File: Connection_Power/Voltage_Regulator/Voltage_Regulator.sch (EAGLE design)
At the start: 7 parts, among them IC2 TS1117

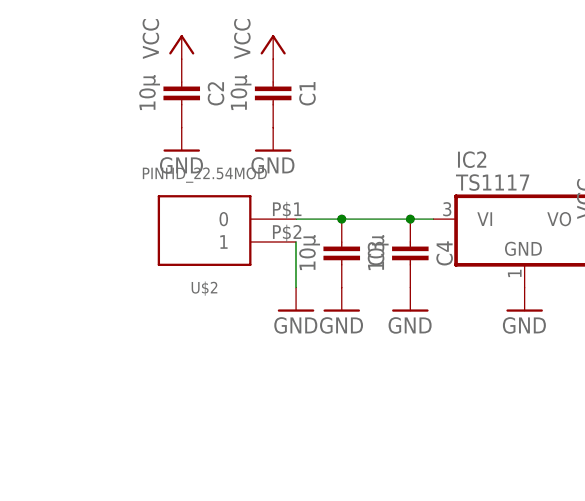
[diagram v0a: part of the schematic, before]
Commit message: Update Pinheader
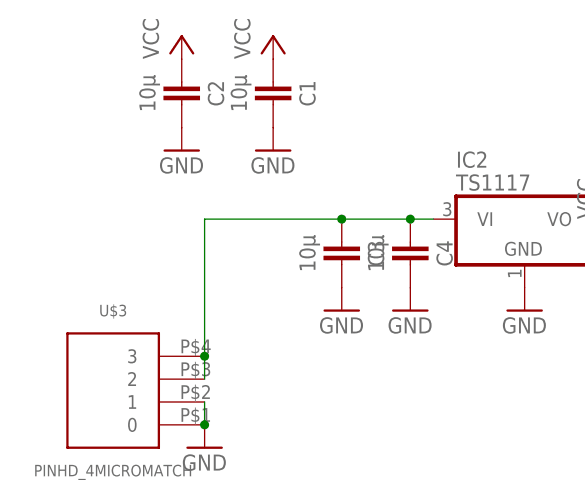
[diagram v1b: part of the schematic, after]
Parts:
- removed U$2: PINHD_22.54MOD, thar:PINHD_22.54MOD
- added U$3: PINHD_4MICROMATCH, thar:PINHD_4MICROMATCH
- C1, C2, C3, C4: device thar:CAPACITOR1206 -> thar:CAPACITOR
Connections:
- net GND: now also U$3.0, U$3.1; no longer U$2.1
- net N$2: now also U$3.2, U$3.3; no longer U$2.0
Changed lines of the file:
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@@
 <grid distance="0.1" unitdist="inch" unit="inch" style="lines" multiple="1" display="no" altdistance="0.01" altunitdist="inch" altunit="inch"/>
 <layers>
-<layer number="1" name="Top" color="4" fill="1" visible="yes" active="no"/>
-<layer number="16" name="Bottom" color="1" fill="1" visible="yes" active="no"/>
-<layer number="17" name="Pads" color="2" fill="1" visible="yes" active="no"/>
-<layer number="18" name="Vias" color="2" fill="1" visible="yes" active="no"/>
-<layer number="19" name="Unrouted" color="6" fill="1" visible="yes" active="no"/>
-<layer number="20" name="Dimension" color="15" fill="1" visible="yes" active="no"/>
-<layer number="21" name="tPlace" color="7" fill="1" visible="yes" active="no"/>
-<layer number="22" name="bPlace" color="7" fill="1" visible="yes" active="no"/>
-<layer number="23" name="tOrigins" color="15" fill="1" visible="yes" active="no"/>
-<layer number="24" name="bOrigins" color="15" fill="1" visible="yes" active="no"/>
-<layer number="25" name="tNames" color="7" fill="1" visible="yes" active="no"/>
-<layer number="26" name="bNames" color="7" fill="1" visible="yes" active="no"/>
-<layer number="27" name="tValues" color="7" fill="1" visible="yes" active="no"/>
-<layer number="28" name="bValues" color="7" fill="1" visible="yes" active="no"/>
+<layer number="1" name="Top" color="4" fill="1" visible="no" active="no"/>
+<layer number="16" name="Bottom" color="1" fill="1" visible="no" active="no"/>
+<layer number="17" name="Pads" color="2" fill="1" visible="no" active="no"/>
+<layer number="18" name="Vias" color="2" fill="1" visible="no" active="no"/>
+<layer number="19" name="Unrouted" color="6" fill="1" visible="no" active="no"/>
+<layer number="20" name="Dimension" color="15" fill="1" visible="no" active="no"/>
+<layer number="21" name="tPlace" color="7" fill="1" visible="no" active="no"/>
+<layer number="22" name="bPlace" color="7" fill="1" visible="no" active="no"/>
+<layer number="23" name="tOrigins" color="15" fill="1" visible="no" active="no"/>
+<layer number="24" name="bOrigins" color="15" fill="1" visible="no" active="no"/>
+<layer number="25" name="tNames" color="7" fill="1" visible="no" active="no"/>
+<layer number="26" name="bNames" color="7" fill="1" visible="no" active="no"/>
+<layer number="27" name="tValues" color="7" fill="1" visible="no" active="no"/>
+<layer number="28" name="bValues" color="7" fill="1" visible="no" active="no"/>
 <layer number="29" name="tStop" color="7" fill="3" visible="no" active="no"/>
 <layer number="30" name="bStop" color="7" fill="6" visible="no" active="no"/>
@@
 <layer number="35" name="tGlue" color="7" fill="4" visible="no" active="no"/>
 <layer number="36" name="bGlue" color="7" fill="5" visible="no" active="no"/>
-<layer number="37" name="tTest" color="7" fill="1" visible="yes" active="no"/>
-<layer number="38" name="bTest" color="7" fill="1" visible="yes" active="no"/>
+<layer number="37" name="tTest" color="7" fill="1" visible="no" active="no"/>
+<layer number="38" name="bTest" color="7" fill="1" visible="no" active="no"/>
 <layer number="39" name="tKeepout" color="4" fill="11" visible="no" active="no"/>
 <layer number="40" name="bKeepout" color="1" fill="11" visible="no" active="no"/>
@@
 <layer number="44" name="Drills" color="7" fill="1" visible="no" active="no"/>
 <layer number="45" name="Holes" color="7" fill="1" visible="no" active="no"/>
-<layer number="46" name="Milling" color="3" fill="1" visible="yes" active="no"/>
-<layer number="47" name="Measures" color="7" fill="1" visible="yes" active="no"/>
-<layer number="48" name="Document" color="7" fill="1" visible="yes" active="no"/>
-<layer number="49" name="Reference" color="7" fill="1" visible="yes" active="no"/>
-<layer number="50" name="dxf" color="7" fill="1" visible="yes" active="no"/>
-<layer number="51" name="tDocu" color="7" fill="1" visible="yes" active="no"/>
-<layer number="52" name="bDocu" color="7" fill="1" visible="yes" active="no"/>
-<layer number="53" name="tGND_GNDA" color="7" fill="9" visible="yes" active="no"/>
-<layer number="54" name="bGND_GNDA" color="1" fill="9" visible="yes" active="no"/>
-<layer number="56" name="wert" color="7" fill="1" visible="yes" active="no"/>
-<layer number="57" name="tCAD" color="7" fill="1" visible="yes" active="no"/>
+<layer number="46" name="Milling" color="3" fill="1" visible="no" active="no"/>
+<layer number="47" name="Measures" color="7" fill="1" visible="no" active="no"/>
+<layer number="48" name="Document" color="7" fill="1" visible="no" active="no"/>
+<layer number="49" name="Reference" color="7" fill="1" visible="no" active="no"/>
+<layer number="50" name="dxf" color="7" fill="1" visible="no" active="no"/>
+<layer number="51" name="tDocu" color="7" fill="1" visible="no" active="no"/>
+<layer number="52" name="bDocu" color="7" fill="1" visible="no" active="no"/>
+<layer number="53" name="tGND_GNDA" color="7" fill="9" visible="no" active="no"/>
+<layer number="54" name="bGND_GNDA" color="1" fill="9" visible="no" active="no"/>
+<layer number="56" name="wert" color="7" fill="1" visible="no" active="no"/>
+<layer number="57" name="tCAD" color="7" fill="1" visible="no" active="no"/>
+<layer number="90" name="Modules" color="5" fill="1" visible="no" active="no"/>
 <layer number="91" name="Nets" color="2" fill="1" visible="yes" active="yes"/>
 <layer number="92" name="Busses" color="1" fill="1" visible="yes" active="yes"/>
@@
 <layer number="97" name="Info" color="7" fill="1" visible="yes" active="yes"/>
 <layer number="98" name="Guide" color="6" fill="1" visible="yes" active="yes"/>
+<layer number="99" name="SpiceOrder" color="7" fill="1" visible="no" active="no"/>
 <layer number="100" name="Muster" color="7" fill="1" visible="no" active="no"/>
 <layer number="101" name="Patch_Top" color="12" fill="4" visible="yes" active="yes"/>
@@
 <layer number="111" name="LPC17xx" color="7" fill="1" visible="no" active="yes"/>
 <layer number="112" name="tSilk" color="7" fill="1" visible="no" active="yes"/>
+<layer number="113" name="IDFDebug" color="7" fill="1" visible="yes" active="yes"/>
 <layer number="116" name="Patch_BOT" color="9" fill="4" visible="yes" active="yes"/>
 <layer number="118" name="Rect_Pads" color="7" fill="1" visible="no" active="yes"/>
@@
 <part name="GND2" library="supply1" deviceset="GND" device=""/>
 <part name="P+3" library="supply1" deviceset="VCC" device=""/>
-<part name="C2" library="thar" deviceset="CAPACITOR" device="1206" value="10µ"/>
-<part name="GND4" library="supply1" deviceset="GND" device=""/>
-<part name="C3" library="thar" deviceset="CAPACITOR" device="1206" value="10µ"/>
+<part name="C2" library="thar" deviceset="CAPACITOR" device="" value="10µ"/>
+<part name="C3" library="thar" deviceset="CAPACITOR" device="" value="10µ"/>
 <part name="GND5" library="supply1" deviceset="GND" device=""/>
 <part name="P+4" library="supply1" deviceset="VCC" device=""/>
 <part name="GND3" library="supply1" deviceset="GND" device=""/>
-<part name="C1" library="thar" deviceset="CAPACITOR" device="1206" value="10µ"/>
-<part name="C4" library="thar" deviceset="CAPACITOR" device="1206" value="10µ"/>
+<part name="C1" library="thar" deviceset="CAPACITOR" device="" value="10µ"/>
+<part name="C4" library="thar" deviceset="CAPACITOR" device="" value="10µ"/>
 <part name="GND7" library="supply1" deviceset="GND" device=""/>
 <part name="IC2" library="welectronic" deviceset="TS1117" device=""/>
 <part name="GND6" library="supply1" deviceset="GND" device=""/>
-<part name="U$2" library="thar" deviceset="PINHD_2" device="2.54MOD"/>
+<part name="U$3" library="thar" deviceset="PINHD_4" device="MICROMATCH"/>
+<part name="GND8" library="supply1" deviceset="GND" device=""/>
 </parts>
 <sheets>
@@
 <instance part="P+3" gate="VCC" x="73.66" y="104.14"/>
 <instance part="C2" gate="G$1" x="25.4" y="114.3" rot="R270"/>
-<instance part="GND4" gate="1" x="38.1" y="91.44"/>
 <instance part="C3" gate="G$1" x="43.18" y="96.52" rot="R270"/>
 <instance part="GND5" gate="1" x="43.18" y="91.44"/>
@@
 <instance part="IC2" gate="G$1" x="63.5" y="101.6"/>
 <instance part="GND6" gate="1" x="63.5" y="91.44"/>
-<instance part="U$2" gate="G$1" x="27.94" y="99.06" rot="MR0"/>
+<instance part="U$3" gate="G$1" x="17.78" y="81.28" rot="R180"/>
+<instance part="GND8" gate="1" x="27.94" y="76.2"/>
 </instances>
 <busses>
@@
 </segment>
 <segment>
-<pinref part="GND4" gate="1" pin="GND"/>
-<wire x1="38.1" y1="99.06" x2="38.1" y2="93.98" width="0.1524" layer="91"/>
-<pinref part="U$2" gate="G$1" pin="1"/>
-</segment>
-<segment>
 <pinref part="C3" gate="G$1" pin="2"/>
 <pinref part="GND5" gate="1" pin="GND"/>
@@
 <pinref part="IC2" gate="G$1" pin="GND"/>
 <pinref part="GND6" gate="1" pin="GND"/>
+</segment>
+<segment>
+<pinref part="U$3" gate="G$1" pin="0"/>
+<pinref part="U$3" gate="G$1" pin="1"/>
+<wire x1="27.94" y1="78.74" x2="27.94" y2="81.28" width="0.1524" layer="91"/>
+<pinref part="GND8" gate="1" pin="GND"/>
+<junction x="27.94" y="78.74"/>
 </segment>
 </net>
@@
 <pinref part="C3" gate="G$1" pin="1"/>
 <wire x1="50.8" y1="101.6" x2="43.18" y2="101.6" width="0.1524" layer="91"/>
-<wire x1="43.18" y1="101.6" x2="38.1" y2="101.6" width="0.1524" layer="91"/>
 <junction x="43.18" y="101.6"/>
 <pinref part="C4" gate="G$1" pin="1"/>
 <junction x="50.8" y="101.6"/>
 <pinref part="IC2" gate="G$1" pin="VI"/>
-<pinref part="U$2" gate="G$1" pin="0"/>
+<pinref part="U$3" gate="G$1" pin="2"/>
+<pinref part="U$3" gate="G$1" pin="3"/>
+<wire x1="27.94" y1="83.82" x2="27.94" y2="86.36" width="0.1524" layer="91"/>
+<wire x1="43.18" y1="101.6" x2="27.94" y2="101.6" width="0.1524" layer="91"/>
+<wire x1="27.94" y1="101.6" x2="27.94" y2="86.36" width="0.1524" layer="91"/>
+<junction x="27.94" y="86.36"/>
 </segment>
 </net>
